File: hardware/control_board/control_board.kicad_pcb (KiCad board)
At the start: 2 copper layers, 286 x 99.4 mm, 125 parts, among them IC1 24LC512, IC10 ATMEGA644p, IC2 74HC165, IC3 74HC165, IC4 4051, IC5 4051, IC6 4051, IC7 4051, IC8 74HC595, IC9 74HC165, J1 Conn_01x08, J2 Conn_01x06, Q1 20MHz, SW1 Encoder, U1 AVR ISP, X1 MIDI, X2 MIDI

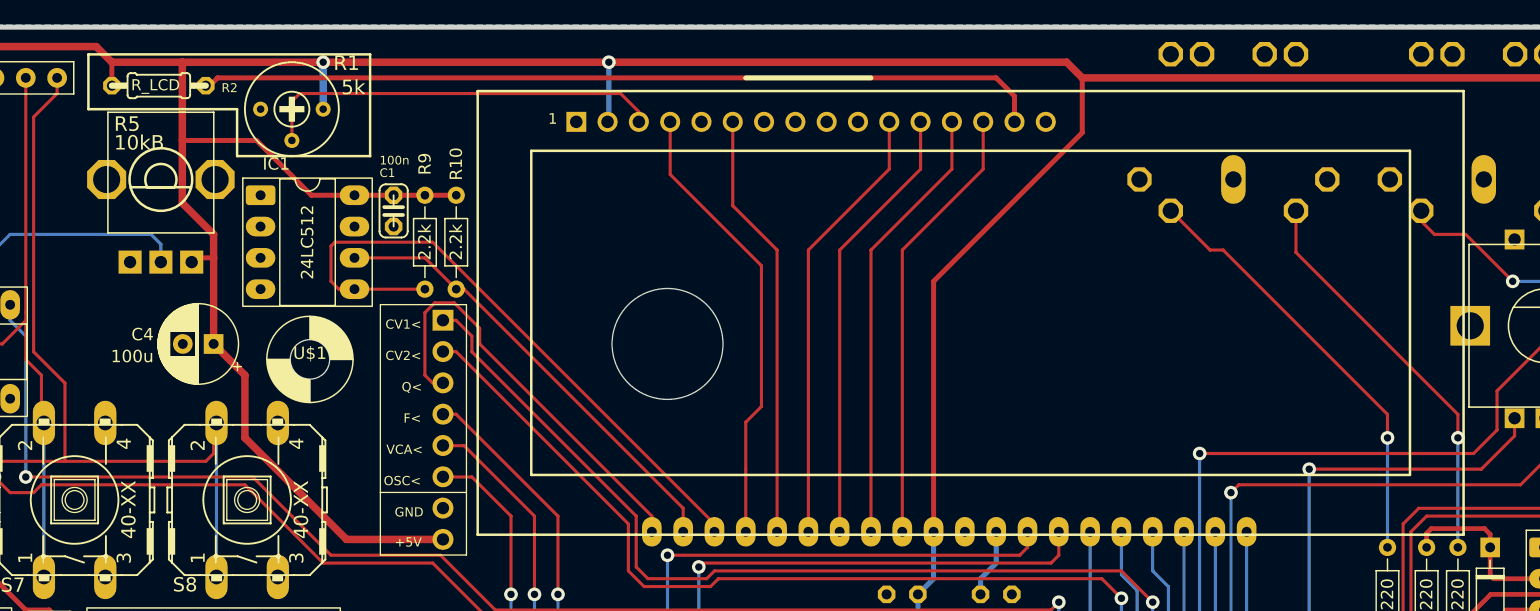
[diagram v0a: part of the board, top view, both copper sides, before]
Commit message: update symbol and footprint for display
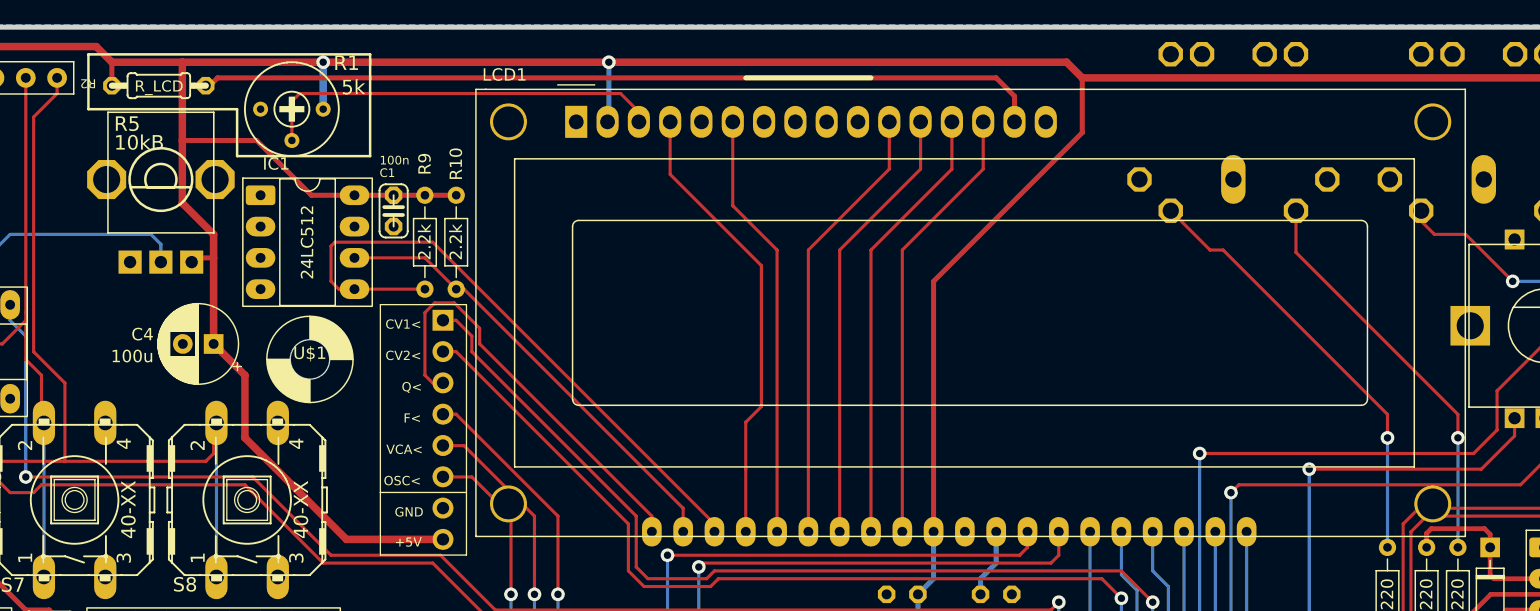
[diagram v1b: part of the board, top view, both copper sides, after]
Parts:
- removed LCD0: LCD-16X2, shruthi_control_board_xt_v03:LCD-16X2
- removed UNK_HOLE_0: , shruthi_control_board_xt_v03:dummyfp0
- added LCD1: WC1602A, Display:WC1602A, F.Cu at (181.6, 101.4)
- turned R2 to 180 degrees
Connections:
- net /shruthi_control_board_xt_v03_1/CV1 renamed /mcu/CV1
- net /shruthi_control_board_xt_v03_1/CV2 renamed /mcu/CV2
- net /shruthi_control_board_xt_v03_1/CVF renamed /mcu/CVF
- net /shruthi_control_board_xt_v03_1/CVG renamed /mcu/CVG
- net /shruthi_control_board_xt_v03_1/CVQ renamed /mcu/CVQ
- net /shruthi_control_board_xt_v03_1/EXT_TX renamed /mcu/EXT_TX
- net /shruthi_control_board_xt_v03_1/MIDI_RX renamed /mcu/MIDI_RX
- net /shruthi_control_board_xt_v03_1/MIDI_TX renamed /mcu/MIDI_TX
- net /shruthi_control_board_xt_v03_1/OSC renamed /mcu/OSC
- net /shruthi_control_board_xt_v03_1/RESET renamed /mcu/RESET
- net /shruthi_control_board_xt_v03_1/SCL renamed /mcu/SCL
- net /shruthi_control_board_xt_v03_1/SDA renamed /mcu/SDA
- net /shruthi_control_board_xt_v03_1/XTAL1 renamed /mcu/XTAL1
- net /shruthi_control_board_xt_v03_1/XTAL2 renamed /mcu/XTAL2
- net /shruthi_control_board_xt_v03_2/CUTOFF renamed /pots/CUTOFF
- net /shruthi_control_board_xt_v03_2/EDIT1 renamed /pots/EDIT1
- net /shruthi_control_board_xt_v03_2/EDIT2 renamed /pots/EDIT2
- net /shruthi_control_board_xt_v03_2/EDIT3 renamed /pots/EDIT3
- net /shruthi_control_board_xt_v03_2/EDIT4 renamed /pots/EDIT4
- net /shruthi_control_board_xt_v03_2/ENV1_ATTACK renamed /pots/ENV1_ATTACK
- net /shruthi_control_board_xt_v03_2/ENV1_DECAY renamed /pots/ENV1_DECAY
- net /shruthi_control_board_xt_v03_2/ENV1_RELEASE renamed /pots/ENV1_RELEASE
- net /shruthi_control_board_xt_v03_2/ENV1_SUSTAIN renamed /pots/ENV1_SUSTAIN
- net /shruthi_control_board_xt_v03_2/ENV2_ATTACK renamed /pots/ENV2_ATTACK
- net /shruthi_control_board_xt_v03_2/ENV2_DECAY renamed /pots/ENV2_DECAY
- net /shruthi_control_board_xt_v03_2/ENV2_RELEASE renamed /pots/ENV2_RELEASE
- net /shruthi_control_board_xt_v03_2/ENV2_SUSTAIN renamed /pots/ENV2_SUSTAIN
- net /shruthi_control_board_xt_v03_2/FILTER_ENV renamed /pots/FILTER_ENV
- net /shruthi_control_board_xt_v03_2/FILTER_LFO renamed /pots/FILTER_LFO
- net /shruthi_control_board_xt_v03_2/LFO1_ATTACK renamed /pots/LFO1_ATTACK
- net /shruthi_control_board_xt_v03_2/LFO1_RATE renamed /pots/LFO1_RATE
- net /shruthi_control_board_xt_v03_2/LFO2_ATTACK renamed /pots/LFO2_ATTACK
- net /shruthi_control_board_xt_v03_2/LFO2_RATE renamed /pots/LFO2_RATE
- net /shruthi_control_board_xt_v03_2/MIX_BALANCE renamed /pots/MIX_BALANCE
- net /shruthi_control_board_xt_v03_2/MIX_NOISE renamed /pots/MIX_NOISE
- net /shruthi_control_board_xt_v03_2/MIX_SUB renamed /pots/MIX_SUB
- net /shruthi_control_board_xt_v03_2/OSC1_PARAMETER renamed /pots/OSC1_PARAMETER
- net /shruthi_control_board_xt_v03_2/OSC1_RANGE renamed /pots/OSC1_RANGE
- net /shruthi_control_board_xt_v03_2/OSC2_DETUNE renamed /pots/OSC2_DETUNE
- net /shruthi_control_board_xt_v03_2/OSC2_PARAMETER renamed /pots/OSC2_PARAMETER
- net /shruthi_control_board_xt_v03_2/OSC2_RANGE renamed /pots/OSC2_RANGE
- net /shruthi_control_board_xt_v03_2/RESONANCE renamed /pots/RESONANCE
- net /shruthi_control_board_xt_v03_2/VOLUME renamed /pots/VOLUME
- net /shruthi_control_board_xt_v03_3/INPUT_CHAIN_1 renamed /buttons/INPUT_CHAIN_1
- net /shruthi_control_board_xt_v03_3/INPUT_CHAIN_2 renamed /buttons/INPUT_CHAIN_2
- R2 pad 1: VCC -> Net-(LCD1-LED(+))
- R2 pad 2: Net-(LCD1-LEDA) -> VCC
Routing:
- net Net-(LCD1-LED(+)): track 0.00 -> 68.6 mm
- net Net-(LCD0-A): track 68.6 -> 0.00 mm
- net unconnected-(R30-Pad2): track 0.00 -> 57.2 mm
- net /pots/ENV2_RELEASE: track 57.2 -> 0.00 mm
- net Net-(LCD1-VO): track 0.00 -> 33.0 mm
- net Net-(LCD0-VO): track 33.0 -> 0.00 mm

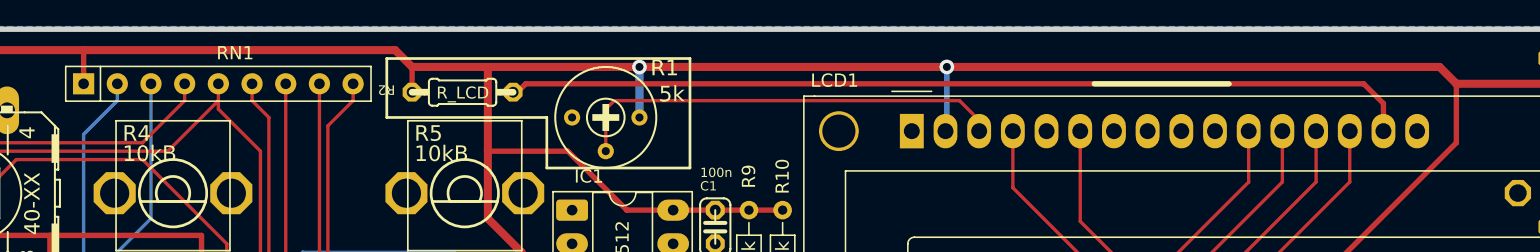
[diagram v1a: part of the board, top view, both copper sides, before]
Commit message: update lcd LED and trimmer footprints
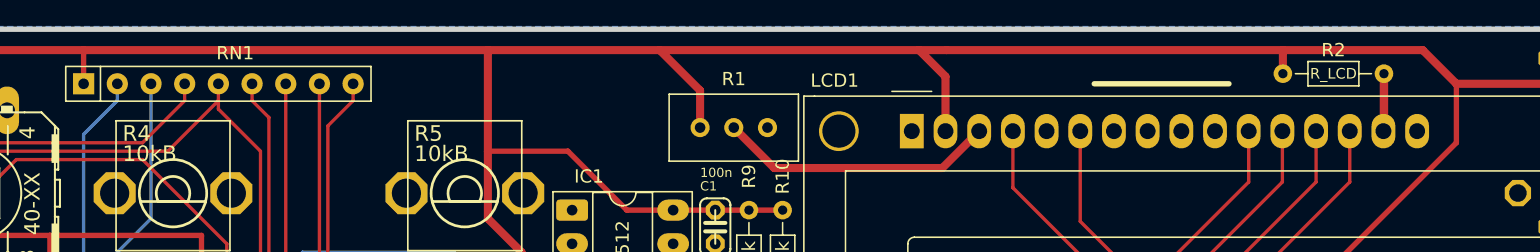
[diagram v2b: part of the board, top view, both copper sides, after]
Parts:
- R1: footprint shruthi_control_board_xt_v03:RTRIM3339P -> Potentiometer_THT:Potentiometer_Bourns_3296W_Vertical
- R2: footprint shruthi_control_board_xt_v03:0204_7 -> Resistor_THT:R_Axial_DIN0204_L3.6mm_D1.6mm_P7.62mm_Horizontal
- moved R2 69.5 mm to (217.2, 97.0)
- moved R1 12.2 mm to (170.7, 101.1)
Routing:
- net Net-(LCD1-LED(+)): track 68.6 -> 4.35 mm
- net Net-(LCD1-VO): track 33.0 -> 21.7 mm
- net VCC: track 1497.9 -> 1504.5 mm, vias 6 -> 4
